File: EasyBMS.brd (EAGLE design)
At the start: 32 x 100 mm, 143 parts, among them Q1 BSS84LT1G, Q10 BSS84LT1G, Q11 BSS84LT1G, Q12 BSS84LT1G, Q14 BSS84LT1G, Q3 BSS84LT1G, Q4 BSS84LT1G, Q5 BSS84LT1G, Q6 BSS84LT1G, Q7 BSS84LT1G, Q8 BSS84LT1G, Q9 BSS84LT1G

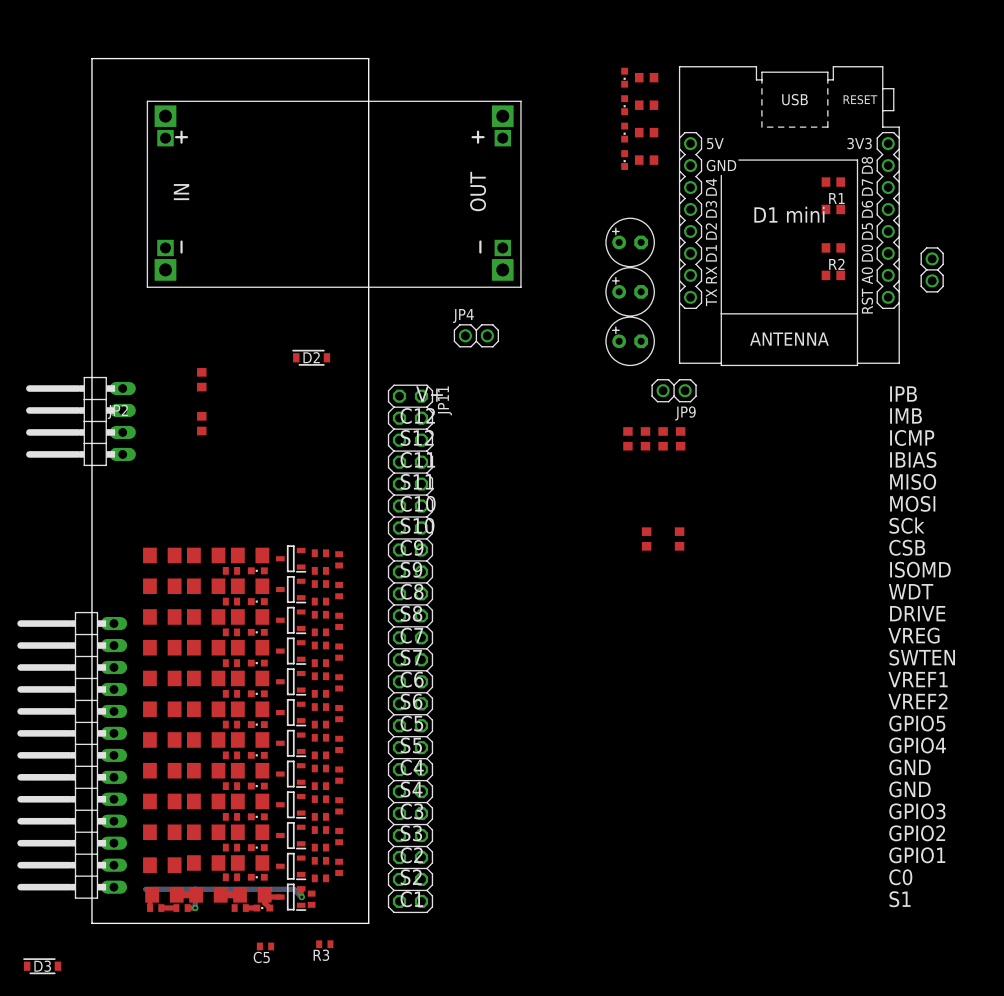
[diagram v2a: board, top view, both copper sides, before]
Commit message: size changed to 100x49
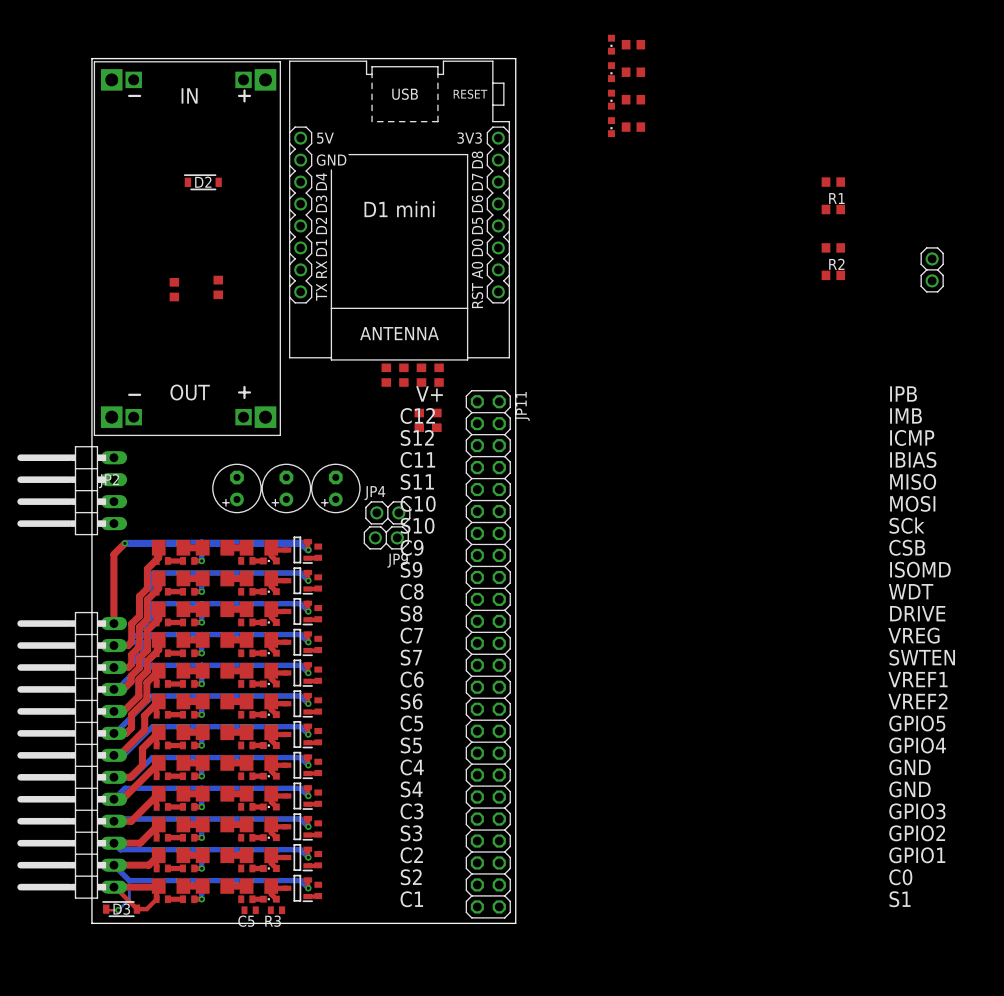
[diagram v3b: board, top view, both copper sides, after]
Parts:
- removed C4: (no value), rcl:C0402
- removed LED10, LED18: KT-0603R, led:CHIPLED_0603
- removed Q1, Q14: BSS84LT1G, SamacSys_Parts:SOT96P237X111-3N
- removed R100, R19: 100R, rcl:R0402
- removed R13, R98: 3.3k, rcl:R0402
- removed R17, R18, R9, R96, R97: 10R0, rcl:R1206
- removed R82, R99: 470R, rcl:R0402
- added C16: (no value), rcl:C0402
- added LED17, LED5: KT-0603R, led:CHIPLED_0603
- added Q13, Q2: BSS84LT1G, SamacSys_Parts:SOT96P237X111-3N
- added R10, R93: 3.3k, rcl:R0402
- added R11, R94: 470R, rcl:R0402
- added R4, R7, R8, R90, R91, R92: 10R0, rcl:R1206
- added R89: 100R, rcl:R0402
- R12, R24, R30, R36, R42, R48, R64, R70, R76, R83, R95: value 10R0 -> 100R; device rcl:R1206 -> rcl:R0402
- R21, R27, R33, R39, R45, R51, R67, R73, R79, R86: value 3.3k -> 10R0; device rcl:R0402 -> rcl:R1206
- R22, R28, R34, R40, R46, R52, R68, R74, R80, R87: value 470R -> 3.3k
- R23, R29, R35, R41, R47, R63, R69, R75, R81, R88: value 100R -> 470R
- moved C1 53.6 mm to (16.8, 50.3), turned to 90 degrees
- moved C3 45.8 mm to (22.5, 50.3), turned to 90 degrees
- moved U$2 45.1 mm to (35.6, 82.5)
- moved C2 38.1 mm to (28.2, 50.3), turned to 90 degrees
- moved JP9 37.4 mm to (34.0, 44.6)
- moved R6 33.1 mm to (37.8, 58.2)
- moved R59 28.9 mm to (38.1, 63.4)
- moved R60 28.9 mm to (40.1, 63.4)
- moved R15 28.9 mm to (36.1, 63.4)
- moved R16 28.9 mm to (34.0, 63.4)
- moved R5 27.9 mm to (39.9, 58.2), turned to 270 degrees
- moved C12 25.0 mm to (8.13, 24.1), turned to 180 degrees
- moved D2 23.8 mm to (12.9, 85.7)
- moved C14 23.1 mm to (8.13, 31.2), turned to 180 degrees
- moved JP4 22.9 mm to (34.2, 47.5)
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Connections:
- removed net C: C4.1, R19.1
- removed net LOWER: C4.2, R17.1, R82.2
- removed net N$15: R18.2, R9.1
- removed net N$157: LED10.C, R82.1
- removed net N$17: R17.2, R18.1
- removed net N$18: LED10.A, Q1.3, R9.2
- removed net N$25: Q1.1, R13.2
- removed net N$27 (its old number): LED7.A, Q4.3, R26.2
- removed net N$33 (its old number): LED8.A, Q5.3, R32.2
- removed net N$38 (its old number): LED9.A, Q6.3, R38.2
- removed net N$43 (its old number): LED11.A, Q7.3, R44.2
- removed net N$48 (its old number): LED12.A, Q8.3, R50.2
- removed net N$53 (its old number): LED13.A, Q9.3, R66.2
- removed net N$58 (its old number): LED14.A, Q10.3, R72.2
- removed net N$7: R3.2
- removed net N$79: R95.2, R96.1
- removed net N$80: R96.2, R97.1
- removed net N$81: LED18.A, Q14.3, R97.2
- removed net N$82: Q14.1, R98.2
- removed net N$83: LED18.C, R99.1
- removed net S: R13.1
- removed net UPPERCELL: Q1.2, R19.2
- new net N$10: LED5.A, Q2.3, R8.2
- new net N$11: Q2.1, R10.2
- new net N$12: LED5.C, R11.1
- new net N$16: LED6.A, Q3.3, R21.2
- new net N$24: Q4.1, R28.2
- new net N$26: LED7.C, R29.1
- new net N$32: LED8.C, R35.1
- new net N$37: LED9.C, R41.1
- new net N$42: LED11.C, R47.1
- new net N$47: LED12.C, R63.1
- new net N$52: LED13.C, R69.1
- new net N$57: LED14.C, R75.1
- new net N$61: Q11.1, R80.2
- new net N$68: R90.2, R91.1
- new net N$74: LED17.C, R94.1
- new net N$8: R4.2, R7.1
- new net N$9: R7.2, R8.1
- net C1: now also C6.1, R12.1
- net C10: now also C15.1, R83.1; no longer C17.1, R100.1
- net C11: now also C16.1, R89.1; no longer C12.1, R69.1
- net C12: now also C17.1, R95.1; no longer C14.1, R81.1
- net C2: now also C7.1, R24.1; no longer C6.1, R23.1
- net C3: now also C9.1, R36.1; no longer C7.1, R29.1
- net C4: now also R30.1; no longer R35.1
- net C5: now also C10.1, R42.1; no longer C9.1, R41.1
- net C6: now also C11.1, R48.1; no longer C10.1, R47.1
- net C7: now also C12.1, R64.1; no longer C11.1, R63.1
- net C8: now also R70.1; no longer R75.1
- net C9: now also C14.1, R76.1; no longer C15.1, R88.1
- net GND: now also C5.2, C6.2, D3.2, R11.2, R3.2, R4.1
- net N$14: now also R20.2, R21.1; no longer R12.2, R14.1
- net N$19: now also Q3.1, R22.2; no longer LED6.A, Q3.3, R20.2
- net N$20: now also LED6.C, R23.1; no longer Q3.1, R21.2
- net N$22: now also R26.2, R27.1; no longer LED6.C, R22.1
- net N$23: now also LED7.A, Q4.3, R27.2; no longer R24.2, R25.1
- net N$28: now also R32.2, R33.1; no longer Q4.1, R27.2
- net N$29: now also LED8.A, Q5.3, R33.2; no longer LED7.C, R28.1
- net N$31: now also Q5.1, R34.2; no longer R30.2, R31.1
- net N$34: now also R38.2, R39.1; no longer Q5.1, R33.2
- net N$35: now also LED9.A, Q6.3, R39.2; no longer LED8.C, R34.1
- net N$36: now also Q6.1, R40.2; no longer R36.2, R37.1
- net N$39: now also R44.2, R45.1; no longer Q6.1, R39.2
- net N$40: now also LED11.A, Q7.3, R45.2; no longer LED9.C, R40.1
- net N$41: now also Q7.1, R46.2; no longer R42.2, R43.1
- net N$44: now also R50.2, R51.1; no longer Q7.1, R45.2
- net N$45: now also LED12.A, Q8.3, R51.2; no longer LED11.C, R46.1
- net N$46: now also Q8.1, R52.2; no longer R48.2, R49.1
- net N$49: now also R66.2, R67.1; no longer Q8.1, R51.2
- net N$50: now also LED13.A, Q9.3, R67.2; no longer LED12.C, R52.1
- net N$51: now also Q9.1, R68.2; no longer R64.2, R65.1
- net N$54: now also R72.2, R73.1; no longer Q9.1, R67.2
- net N$55: now also LED14.A, Q10.3, R73.2; no longer LED13.C, R68.1
- net N$56: now also Q10.1, R74.2; no longer R70.2, R71.1
- net N$59: now also R78.2, R79.1; no longer Q10.1, R73.2
- net N$60: now also LED15.A, Q11.3, R79.2; no longer LED14.C, R74.1
- net N$62: now also LED15.C, R81.1; no longer R76.2, R77.1
- net N$64: now also R85.2, R86.1; no longer LED15.A, Q11.3, R78.2
- net N$65: now also LED16.A, Q12.3, R86.2; no longer Q11.1, R79.2
- net N$66: now also Q12.1, R87.2; no longer LED15.C, R80.1
- net N$67: now also LED16.C, R88.1; no longer R83.2, R84.1
- net N$69: now also R91.2, R92.1; no longer LED16.A, Q12.3, R85.2
- net N$71: now also LED17.A, Q13.3, R92.2; no longer Q12.1, R86.2
- net N$72: now also Q13.1, R93.2; no longer LED16.C, R87.1
- net P10: now also C15.2, Q10.2, R76.2, R77.1, R81.2; no longer C17.2, Q12.2, R88.2, R95.1, R99.2
- net P11: now also C16.2, Q11.2, R83.2, R84.1, R88.2; no longer C12.2, Q14.2, R100.2, R64.1, R68.2
- net P12: now also C17.2, Q12.2, R89.2, R90.1, R94.2; no longer C14.2, Q9.2, R69.2, R76.1, R80.2
- net P13: now also Q13.2, R95.2; no longer Q11.2, R81.2
- net P2: now also C7.2, D3.1, Q2.2, R12.2, R14.1, R23.2; no longer C6.2, R12.1, R22.2
- net P3: now also C9.2, R24.2, R31.1, R35.2; no longer C7.2, R23.2, R24.1, R28.2
- net P4: now also Q5.2, R25.1, R36.2; no longer Q4.2, R30.1, R34.2
- net P5: now also C10.2, Q4.2, R30.2, R37.1, R41.2; no longer C9.2, Q5.2, R35.2, R36.1, R40.2
- net P6: now also C11.2, R42.2, R43.1, R47.2; no longer C10.2, R41.2, R42.1, R46.2
- net P7: now also C12.2, R48.2, R49.1, R63.2; no longer C11.2, R47.2, R48.1, R52.2
- net P8: now also R64.2, R65.1, R69.2; no longer R63.2, R70.1, R74.2
- net P9: now also C14.2, Q9.2, R70.2, R71.1; no longer C15.2, Q10.2, R83.1, R87.2
- net S1: now also R10.1
- net S10: now also R80.1; no longer R98.1
- net S11: now also R87.1; no longer R67.1
- net S12: now also R93.1; no longer R79.1
- net S2: now also R22.1; no longer R21.1
- net S3: now also R34.1; no longer R27.1
- net S4: now also R28.1; no longer R33.1
- net S5: now also R40.1; no longer R39.1
- net S6: now also R46.1; no longer R45.1
- net S7: now also R52.1; no longer R51.1
- net S8: now also R68.1; no longer R73.1
- net S9: now also R74.1; no longer R86.1
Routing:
- net P13: track 0.00 -> 53.7 mm, vias 0 -> 3
- net P12: track 0.00 -> 49.5 mm, vias 0 -> 2
- net P11: track 0.00 -> 47.7 mm, vias 0 -> 2
- net P10: track 0.00 -> 44.5 mm, vias 0 -> 2
- net P9: track 0.00 -> 42.9 mm, vias 0 -> 2
- net P8: track 0.00 -> 40.5 mm, vias 0 -> 2
- net P2: track 0.00 -> 40.3 mm, vias 0 -> 3
- net P7: track 0.00 -> 38.6 mm, vias 0 -> 2
- net P6: track 0.00 -> 37.9 mm, vias 0 -> 2
- net P5: track 0.00 -> 35.9 mm, vias 0 -> 2
- net P4: track 0.00 -> 35.1 mm, vias 0 -> 2
- net P3: track 0.00 -> 34.9 mm, vias 0 -> 2
- net UPPERCELL: track 22.4 -> 0.00 mm, vias 2 -> 0
- net GND: track 0.00 -> 13.3 mm
- net N$60: track 0.00 -> 4.42 mm
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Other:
- board size 32 x 100 mm -> 49 x 100 mm

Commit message: new 2x20 header used
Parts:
- removed JP11: (no value), pinhead_own:2X24
- removed JP4, JP9: (no value), pinhead_own:1X02
- added JP5: (no value), pinhead:2X20
- moved C1 26.0 mm to (40.1, 38.9), turned to 0 degrees
- moved C2 21.0 mm to (40.1, 33.0), turned to 0 degrees
- moved C3 18.5 mm to (40.1, 44.7), turned to 0 degrees
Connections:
- removed net DRIVE: JP11.22
- removed net N$117: JP9.1, R1.2
- removed net SWTEN: JP11.26
- removed net VREG: JP11.24, JP4.2
- removed net WDT: JP11.20
- net 5VDC: now also JP5.10, R1.2; no longer JP4.1, JP9.2
- net C0: now also JP5.30; no longer JP11.46
- net C1: now also JP5.34; no longer JP11.47
- net C10: now also JP5.11; no longer JP11.11
- net C11: now also JP5.7; no longer JP11.7
- net C12: now also JP5.3; no longer JP11.3
- net C2: now also JP5.38; no longer JP11.43
- net C3: now also JP5.39; no longer JP11.39
- net C4: now also JP5.35; no longer JP11.35
- net C5: now also JP5.31; no longer JP11.31
- net C6: now also JP5.27; no longer JP11.27
- net C7: now also JP5.23; no longer JP11.23
- net C8: now also JP5.19; no longer JP11.19
- net C9: now also JP5.15; no longer JP11.15
- net CSB: now also JP5.8; no longer JP11.16
- net GND: now also JP5.16, JP5.18; no longer JP11.18, JP11.36, JP11.38
- net GPIO1: now also JP5.28; no longer JP11.44
- net GPIO2: now also JP5.26; no longer JP11.42
- net GPIO3: now also JP5.24; no longer JP11.40
- net GPIO4: now also JP5.22; no longer JP11.34
- net GPIO5: now also JP5.20; no longer JP11.32
- net ICMP: no longer JP11.6, JP11.8
- net IMB: no longer JP11.4
- net IPB: no longer JP11.2
- net MISO: now also JP5.2; no longer JP11.10
- net MOSI: now also JP5.4; no longer JP11.12
- net P13: now also JP5.1; no longer JP11.1
- net S1: now also JP5.32; no longer JP11.48
- net S10: now also JP5.13; no longer JP11.13
- net S11: now also JP5.9; no longer JP11.9
- net S12: now also JP5.5; no longer JP11.5
- net S2: now also JP5.36; no longer JP11.45
- net S3: now also JP5.40; no longer JP11.41
- net S4: now also JP5.37; no longer JP11.37
- net S5: now also JP5.33; no longer JP11.33
- net S6: now also JP5.29; no longer JP11.29
- net S7: now also JP5.25; no longer JP11.25
- net S8: now also JP5.21; no longer JP11.21
- net S9: now also JP5.17; no longer JP11.17
- net SCK: now also JP5.6; no longer JP11.14
- net VREF1: now also JP5.12; no longer JP11.28
- net VREF2: now also JP5.14; no longer JP11.30
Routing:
- net P13: track 53.7 -> 0.00 mm, vias 3 -> 0
- net P12: track 49.5 -> 0.00 mm, vias 2 -> 0
- net P11: track 47.7 -> 0.00 mm, vias 2 -> 0
- net P10: track 44.5 -> 0.00 mm, vias 2 -> 0
- net P9: track 42.9 -> 0.00 mm, vias 2 -> 0
- net P8: track 40.5 -> 0.00 mm, vias 2 -> 0
- net P2: track 40.3 -> 0.00 mm, vias 3 -> 0
- net P7: track 38.6 -> 0.00 mm, vias 2 -> 0
- net P6: track 37.9 -> 0.00 mm, vias 2 -> 0
- net P5: track 35.9 -> 0.00 mm, vias 2 -> 0
- net P4: track 35.1 -> 0.00 mm, vias 2 -> 0
- net P3: track 34.9 -> 0.00 mm, vias 2 -> 0
- net GND: track 13.3 -> 0.00 mm
- net N$60: track 4.42 -> 0.00 mm
- net N$35: track 4.42 -> 0.00 mm
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
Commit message: positioning
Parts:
- added C18, C19, C4: (no value), rcl:C1206
- moved JP3 74.1 mm to (24.4, 61.7)
- moved LED4 48.1 mm to (31.8, 62.7)
- moved LED3 46.5 mm to (30.2, 62.7)
- moved R2 46.4 mm to (39.9, 82.0)
- moved R61 46.2 mm to (39.9, 84.1)
- moved R62 46.2 mm to (39.9, 80.0)
- moved R1 46.1 mm to (39.9, 78.0)
- moved R56 45.4 mm to (20.1, 85.9)
- moved LED2 45.2 mm to (28.7, 62.7)
- moved R55 45.0 mm to (20.1, 83.8)
- moved R54 44.6 mm to (20.1, 81.8)
- moved R53 44.3 mm to (20.1, 79.8)
- moved LED1 44.1 mm to (27.2, 62.7)
- moved JP2 33.0 mm to (-1.27, 17.0)
- moved C2 24.0 mm to (42.2, 56.9), turned to 90 degrees
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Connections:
- net 5VDC: now also C19.1
- net GND: now also C18.2, C19.2, C4.2
- net VREF1: now also C18.1
- net VREF2: now also C4.1

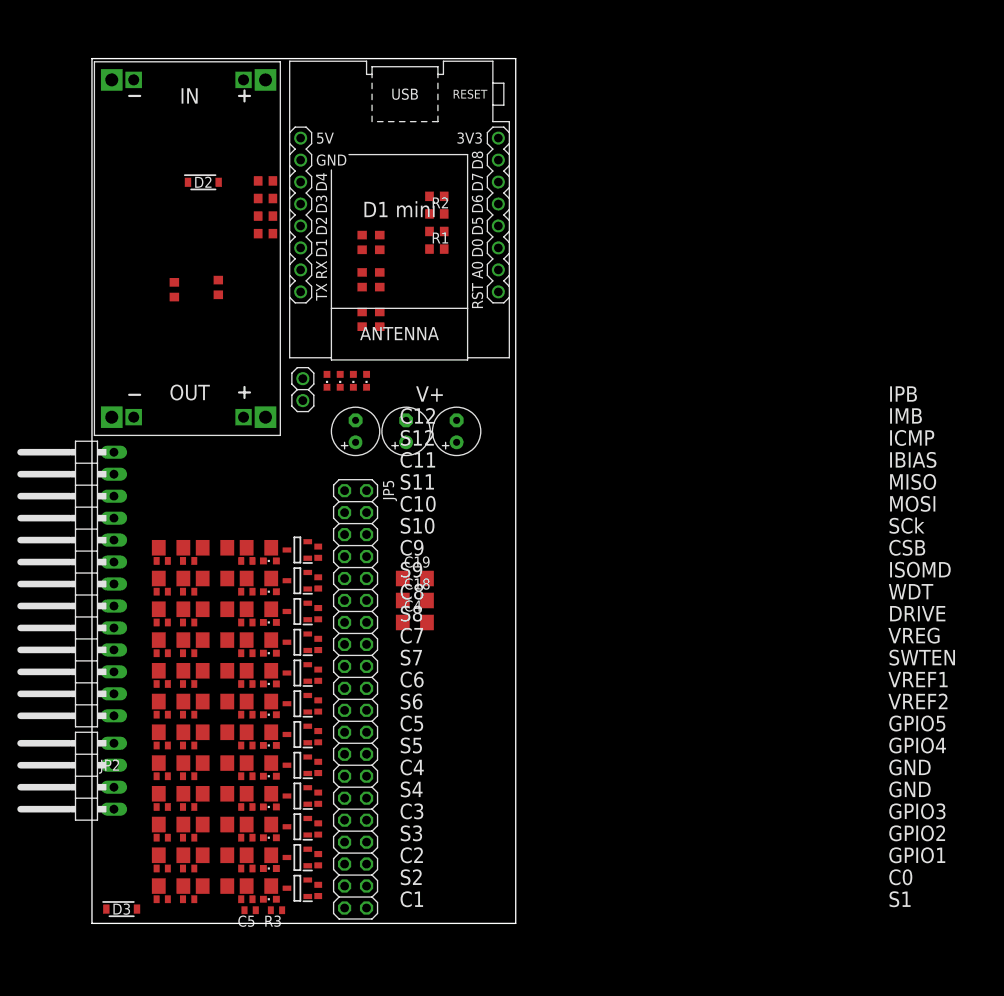
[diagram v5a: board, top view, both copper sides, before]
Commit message: extension ports added
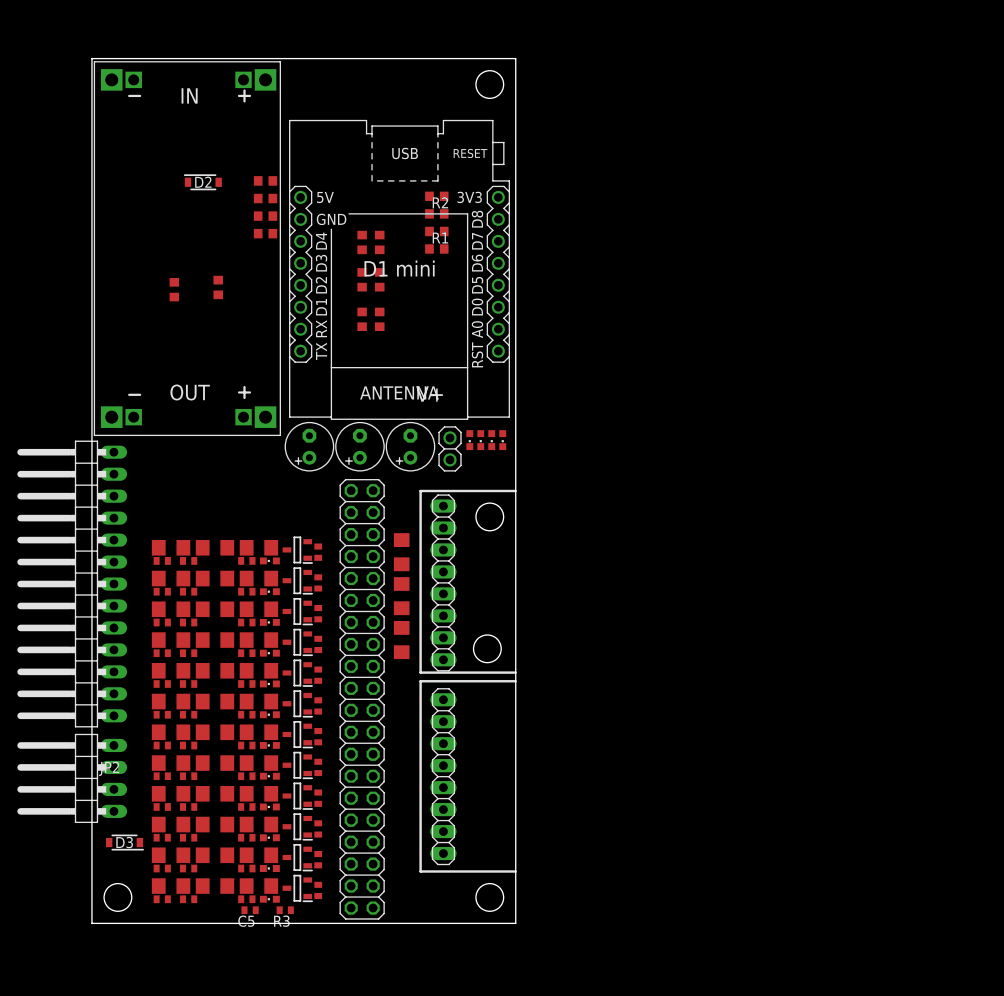
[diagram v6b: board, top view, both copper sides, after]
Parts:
- added JP4, JP6: (no value), pinhead:1X08
- moved JP3 18.3 mm to (41.4, 54.9), turned to 90 degrees
- moved LED1 17.9 mm to (43.7, 55.9)
- moved LED2 17.6 mm to (45.0, 55.9)
- moved LED3 17.4 mm to (46.2, 55.9)
- moved LED4 17.2 mm to (47.5, 55.9)
- moved C2 11.3 mm to (31.0, 55.1)
- moved D3 7.71 mm to (3.76, 9.35), turned to 180 degrees
- moved U$2 6.86 mm to (35.6, 75.7)
- moved C1 5.62 mm to (25.1, 55.1)
- moved C19 3.41 mm to (35.8, 42.9), turned to 90 degrees
- moved C4 2.54 mm to (35.8, 32.8), turned to 270 degrees
- moved C3 1.85 mm to (36.8, 55.1)
- moved C18 1.61 mm to (35.8, 37.8), turned to 90 degrees
- moved R3 1.02 mm to (22.4, 1.52)
- moved JP5 0.76 mm to (31.2, 25.9)
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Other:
- board text removed: "C0"
- board text removed: "C1"
- board text removed: "C10"
- board text removed: "C11"
- board text removed: "C12"
- board text removed: "C2"
- board text removed: "C3"
- board text removed: "C4"
- board text removed: "C5"
- board text removed: "C6"
- board text removed: "C7"
- board text removed: "C8"
- board text removed: "C9"
- board text removed: "CSB"
- board text removed: "DRIVE"
- board text removed: "GND"
- board text removed: "GPIO1"
- board text removed: "GPIO2"
- board text removed: "GPIO3"
- board text removed: "GPIO4"
- board text removed: "GPIO5"
- board text removed: "IBIAS"
- board text removed: "ICMP"
- board text removed: "IMB"
- board text removed: "IPB"
- board text removed: "ISOMD"
- board text removed: "MISO"
- board text removed: "MOSI"
- board text removed: "S1"
- board text removed: "S10"
- board text removed: "S11"
- board text removed: "S12"
- board text removed: "S2"
- board text removed: "S3"
- board text removed: "S4"
- board text removed: "S5"
- board text removed: "S6"
- board text removed: "S7"
- board text removed: "S8"
- board text removed: "S9"
- board text removed: "SCk"
- board text removed: "SWTEN"
- board text removed: "VREF1"
- board text removed: "VREF2"
- board text removed: "VREG"
- board text removed: "WDT"
